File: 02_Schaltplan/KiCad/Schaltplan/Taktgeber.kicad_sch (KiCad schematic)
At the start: 43 parts, among them J3 SPEED (20k-POTI), SW2 MODE, U10 74AHC2G08, U11 NE555, U12 74AHC1G32, U13 74LVC1G175, U14 LTC6993, U15 74LVC1G175, U16 74LVC2G14, U8 74AHC1G14

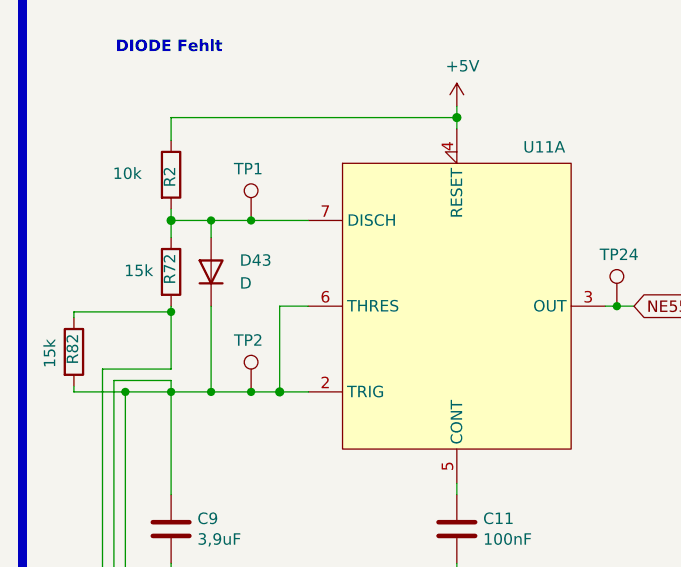
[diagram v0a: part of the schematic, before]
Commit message: ADD
-Dokumentation erweitert
-Schaltplan Fußbeschriftungen
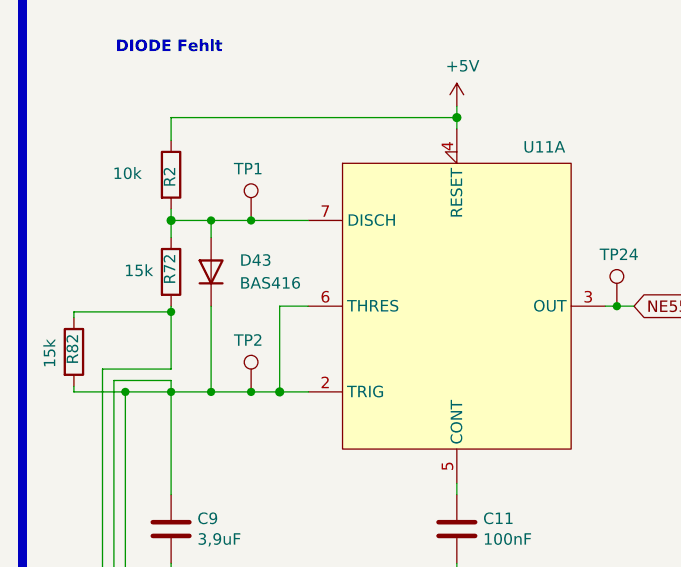
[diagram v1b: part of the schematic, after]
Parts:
- D43: value D -> BAS416; BMK-Nr (none) -> 08-5493
- U10: BMK-Nr - -> 06-0948-1
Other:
- company: (none) -> BMK Group
- title: (none) -> Kabeltester
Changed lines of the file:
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@@
 (kicad_sch (version 20210126) (generator eeschema)
   (paper "A4")
+  (title_block
+    (title "Kabeltester")
+    (company "BMK Group")
+    (comment 1 "Erstellt: Maximilian Hoffmann")
+    (comment 2 "Geprüft: Robert Schulz")
+  )
   (junction (at 28.575 166.37) (diameter 1.016) (color 0 0 0 0))
   (junction (at 28.575 189.23) (diameter 1.016) (color 0 0 0 0))
@@
       (effects (font (size 1.27 1.27)) (justify right))
     )
-    (property "Value" "D" (id 1) (at 43.18 73.66 90)
+    (property "Value" "BAS416" (id 1) (at 43.18 73.66 90)
       (effects (font (size 1.27 1.27)) (justify right))
     )
@@
     )
     (property "Datasheet" "~" (id 3) (at 40.005 72.39 0)
+      (effects (font (size 1.27 1.27)) hide)
+    )
+    (property "BMK-Nr" "08-5493" (id 4) (at 40.005 72.39 90)
       (effects (font (size 1.27 1.27)) hide)
     )
@@
       (effects (font (size 1.27 1.27)) hide)
     )
-    (property "BMK-Nr" "-" (id 4) (at 76.2 193.675 0)
+    (property "BMK-Nr" "06-0948-1" (id 4) (at 76.2 193.675 0)
       (effects (font (size 1.27 1.27)) hide)
     )
@@
       (effects (font (size 1.27 1.27)) hide)
     )
-    (property "BMK-Nr" "-" (id 4) (at 177.8 66.675 0)
+    (property "BMK-Nr" "06-0948-1" (id 4) (at 177.8 66.675 0)
       (effects (font (size 1.27 1.27)) hide)
     )
@@
       (effects (font (size 1.27 1.27)) hide)
     )
-    (property "BMK-Nr" "-" (id 4) (at 177.8 92.075 0)
-      (effects (font (size 1.27 1.27)) hide)
-    )
+    (property "BMK-Nr" "06-0948-1" (id 4) (at 177.8 92.075 0)
+      (effects (font (size 1.27 1.27)) hide)
+    )

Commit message: Changes
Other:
- note added: "Falsch herum"
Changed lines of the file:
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@@
     (effects (font (size 2 2) (thickness 0.4) bold) (justify right bottom))
+  )
+  (text "Falsch herum\n" (at 264.795 45.72 180)
+    (effects (font (size 1.27 1.27)) (justify right bottom))
   )
   (global_label "NE55_OUT" (shape input) (at 86.995 76.2 0)
